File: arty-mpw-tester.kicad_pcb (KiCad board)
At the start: 4 copper layers, 53.3 x 61.5 mm, 144 parts, among them J1 USB4105-GF-A, J10 61300211121, J11 61300211121, J12 61300211121, J14 61300311121, J15 61300311121, J18 61300411121, J19 61300711121, J20 61300411121, J3 arty_chipKIT_connector, J4 61300211121, J5 61300311121, J6 61300211121, J7 61300211121, J8 61300211121, J9 61300211121, Q1 DTC014TEBTL, SW1 JS202011JCQN, SW2 JS202011JCQN, SW3 JS202011JCQN, U1 SN74LVC1G125DCKR, U10 TPD4E02B04DQA, U2 FT232HQ, U3 SN74LVC1G125DCKR, U4 MAX811REUS+T, U5 NTS0102DP, U6 MCP4661-103E/ML, U7 Caravel_breakout_PCB, U8 W25Q32FVSS, U9 MIC2211-AAYML-TR, Y1 ABM8G-12.000MHZ-18-D2Y-T, Y2 ECS-2520MVLC-100-BN-TR

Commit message: Update naming convention
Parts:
- C1, C10, C11, C12, C13, C14, C15, C16, C17, C18, C19, C2, C20, C21, C22, C23, C24, C25, C26, C27, C28, C29, C3, C30, C31, C32, C33, C34, C35, C36, C37, C4, C5, C6, C7, C8, C9: footprint mpw-tester-arty-expansion-footprints:0603-cap -> arty-mpw-tester-footprints:0603-cap
- D1, D2, D3, D4: footprint mpw-tester-arty-expansion-footprints:LED_0603 -> arty-mpw-tester-footprints:LED_0603
- D5, D6, D9: footprint mpw-tester-arty-expansion-footprints:SOD-323F -> arty-mpw-tester-footprints:SOD-323F
- D7, D8: footprint mpw-tester-arty-expansion-footprints:SOD-123 -> arty-mpw-tester-footprints:SOD-123
- J1: footprint mpw-tester-arty-expansion-footprints:GCT_USB4105-GF-A -> arty-mpw-tester-footprints:GCT_USB4105-GF-A
- J10, J11, J12, J4, J6, J7, J8, J9: footprint mpw-tester-arty-expansion-footprints:PinHeader_1x2_P2.54_Drill0.9mm -> arty-mpw-tester-footprints:PinHeader_1x2_P2.54_Drill0.9mm
- J14, J15, J5: footprint mpw-tester-arty-expansion-footprints:PinHeader_1x3_P2.54_Drill1.1mm -> arty-mpw-tester-footprints:PinHeader_1x3_P2.54_Drill1.1mm
- J18, J20: footprint mpw-tester-arty-expansion-footprints:PinHeader_1x4_P2.54mm_Drill1.02mm -> arty-mpw-tester-footprints:PinHeader_1x4_P2.54mm_Drill1.02mm
- J19: footprint mpw-tester-arty-expansion-footprints:61300711121 -> arty-mpw-tester-footprints:61300711121
- J3: footprint mpw-tester-arty-expansion-footprints:ARTY_A7_SHIELD -> arty-mpw-tester-footprints:ARTY_A7_SHIELD
- Q1: footprint mpw-tester-arty-expansion-footprints:SOT-416 -> arty-mpw-tester-footprints:SOT-416
- R1, R10, R11, R12, R13, R14, R15, R16, R17, R18, R19, R2, R20, R21, R22, R23, R24, R25, R26, R27, R28, R29, R3, R30, R31, R32, R33, R34, R35, R6, R7, R8, R9: footprint mpw-tester-arty-expansion-footprints:0603-res -> arty-mpw-tester-footprints:0603-res
- R4, R5: footprint mpw-tester-arty-expansion-footprints:0402-res -> arty-mpw-tester-footprints:0402-res
- S1: footprint mpw-tester-arty-expansion-footprints:SW_SPST_4.2x2.8 -> arty-mpw-tester-footprints:SW_SPST_4.2x2.8
- SW1, SW2, SW3: footprint mpw-tester-arty-expansion-footprints:JS202011JCQN -> arty-mpw-tester-footprints:JS202011JCQN
- TP1: footprint mpw-tester-arty-expansion-footprints:PROBE_PAD_1206 -> arty-mpw-tester-footprints:PROBE_PAD_1206
- U1, U3: footprint mpw-tester-arty-expansion-footprints:SOT-353 -> arty-mpw-tester-footprints:SOT-353
- U10: footprint mpw-tester-arty-expansion-footprints:USON-10_2.5x1.0mm_P0.5mm -> arty-mpw-tester-footprints:USON-10_2.5x1.0mm_P0.5mm
- U2: footprint mpw-tester-arty-expansion-footprints:QFN-48-1EP_8x8mm_P0.5mm_EP6.2x6.2mm_FT232HQ_marking -> arty-mpw-tester-footprints:QFN-48-1EP_8x8mm_P0.5mm_EP6.2x6.2mm_FT232HQ_marking
- U4: footprint mpw-tester-arty-expansion-footprints:SOT-143-4 -> arty-mpw-tester-footprints:SOT-143-4
- U5: footprint mpw-tester-arty-expansion-footprints:TSSOP-8_W3mm -> arty-mpw-tester-footprints:TSSOP-8_W3mm
- U6: footprint mpw-tester-arty-expansion-footprints:QFN-16_EP_4x4_Pitch0.65mm -> arty-mpw-tester-footprints:QFN-16_EP_4x4_Pitch0.65mm
- U7: footprint mpw-tester-arty-expansion-footprints:caravel_breakout -> arty-mpw-tester-footprints:caravel_breakout
- U8: footprint mpw-tester-arty-expansion-footprints:SOIC127P790X216-8N -> arty-mpw-tester-footprints:SOIC127P790X216-8N
- U9: footprint mpw-tester-arty-expansion-footprints:DFN-10-1EP_3x3mm -> arty-mpw-tester-footprints:DFN-10-1EP_3x3mm
- Y1: footprint mpw-tester-arty-expansion-footprints:KX-7 -> arty-mpw-tester-footprints:KX-7
- Y2: footprint mpw-tester-arty-expansion-footprints:Oscillator_SMD_ECS_2520MV-xxx-xx-4Pin_2.5x2.0mm -> arty-mpw-tester-footprints:Oscillator_SMD_ECS_2520MV-xxx-xx-4Pin_2.5x2.0mm

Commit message: Update caravel-breakout footprint with more detailed 3D model and flexypins
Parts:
- G***: footprint antmicro-footprints:antmicro-logo_scaled_12mm_mask -> arty-mpw-tester-footprints:antmicro-logo_scaled_12mm_mask
- G***: footprint antmicro-footprints:antmicro-logo_scaled_12mm -> arty-mpw-tester-footprints:antmicro-logo_scaled_12mm
- REF**: footprint antmicro-footprints:OSHW-Logo_5.7x6mm_Copper -> arty-mpw-tester-footprints:OSHW-Logo_5.7x6mm_Copper
- REF**: footprint antmicro-footprints:OSHW-Logo_5.7x6mm_Mask -> arty-mpw-tester-footprints:OSHW-Logo_5.7x6mm_Mask
- U7: value Caravel_breakout_PCB -> Caravel_breakout_PCB_flexypin; footprint arty-mpw-tester-footprints:caravel_breakout -> arty-mpw-tester-footprints:caravel-breakout-flexypin

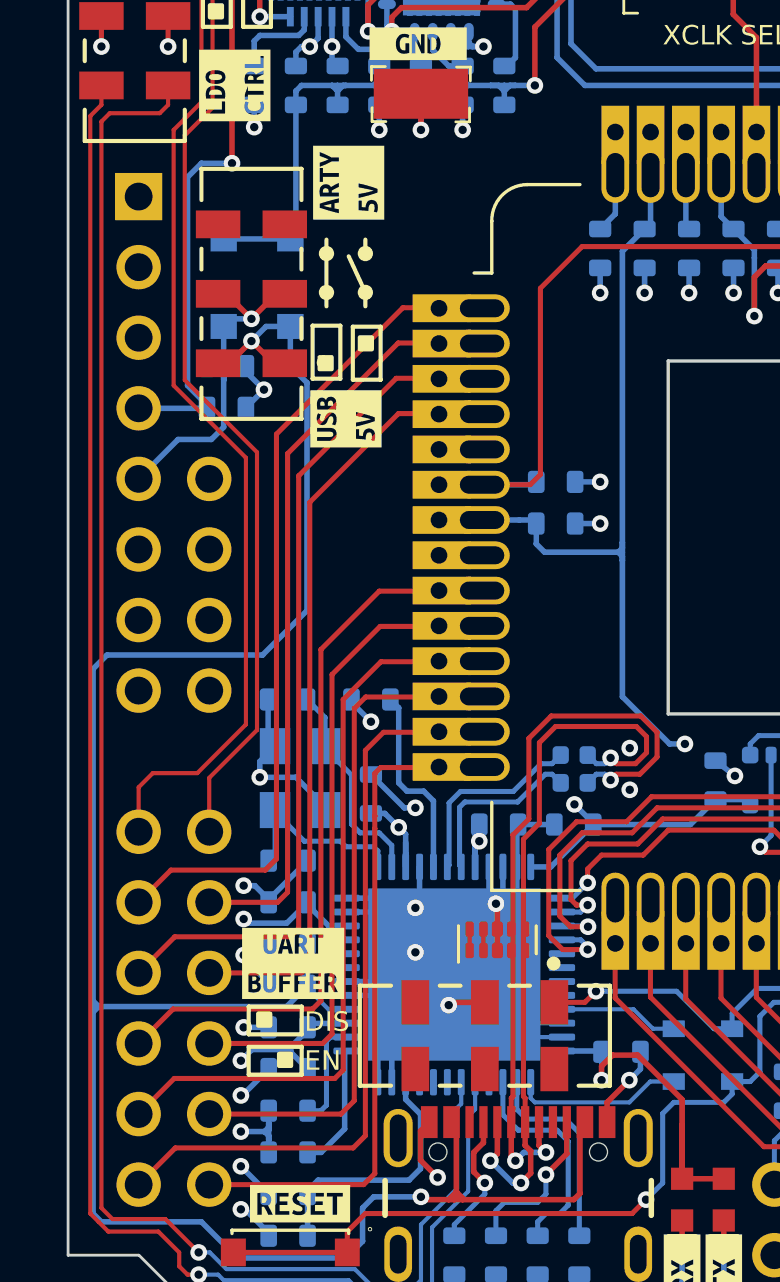
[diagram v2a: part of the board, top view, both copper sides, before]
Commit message: Rotate slide switches so 3D models match default configuration. Update Arty A7 shield connector side
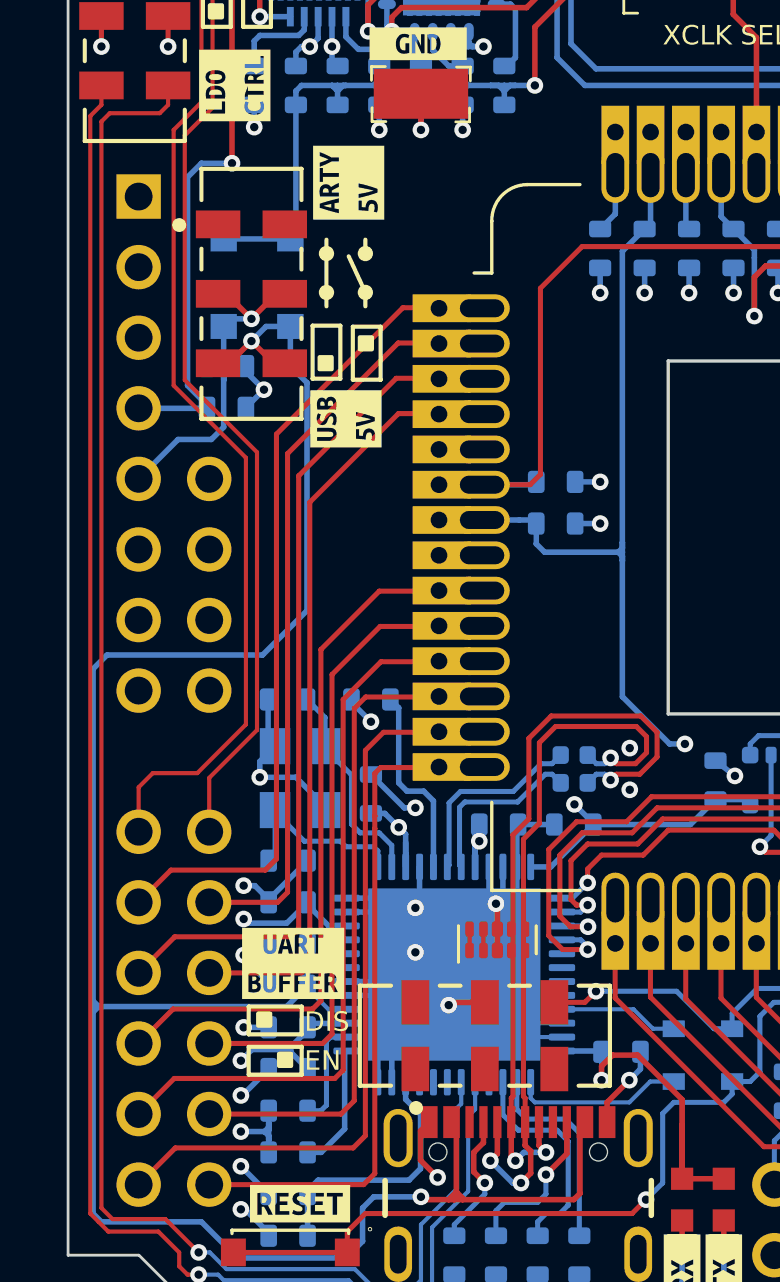
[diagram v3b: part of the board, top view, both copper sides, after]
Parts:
- J3: moved to B.Cu
- turned J3 to 180 degrees
- turned SW2 to 0 degrees
- turned SW3 to -90 degrees
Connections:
- SW2 pad 1: /~{UART_EN} -> unconnected-(SW2-Pad1)
- SW2 pad 2: AGND -> unconnected-(SW2-Pad2)
- SW2 pad 6: unconnected-(SW2-Pad6) -> AGND
- SW2 pad 7: unconnected-(SW2-Pad7) -> /~{UART_EN}
- SW3 pad 1: VBUS -> unconnected-(SW3-Pad1)
- SW3 pad 3: unconnected-(SW3-Pad3) -> VBUS
- SW3 pad 5: VBUS -> unconnected-(SW3-Pad5)
- SW3 pad 7: unconnected-(SW3-Pad7) -> VBUS

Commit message: Add jumper models to the PCB
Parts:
- added REF**: Jumper_1x2_P2.54, arty-mpw-tester-footprints:Jumper_1x2_P2.54, F.Cu at (146.9, 78.9)
- added REF**: Jumper_1x2_P2.54, arty-mpw-tester-footprints:Jumper_1x2_P2.54, F.Cu at (136.3, 67.7)
- added REF**: Jumper_1x2_P2.54, arty-mpw-tester-footprints:Jumper_1x2_P2.54, F.Cu at (124.7, 70.9)
- added REF**: Jumper_1x2_P2.54, arty-mpw-tester-footprints:Jumper_1x2_P2.54, F.Cu at (124.7, 67.7)
- added REF**: Jumper_1x2_P2.54, arty-mpw-tester-footprints:Jumper_1x2_P2.54, F.Cu at (149.5, 67.7)
- added REF**: Jumper_1x2_P2.54, arty-mpw-tester-footprints:Jumper_1x2_P2.54, F.Cu at (141.3, 67.7)
- added REF**: Jumper_1x2_P2.54, arty-mpw-tester-footprints:Jumper_1x2_P2.54, F.Cu at (138.8, 67.7)
- added REF**: Jumper_1x2_P2.54, arty-mpw-tester-footprints:Jumper_1x2_P2.54, F.Cu at (152.1, 67.7)
- added REF**: Jumper_1x2_P2.54, arty-mpw-tester-footprints:Jumper_1x2_P2.54, F.Cu at (147.0, 67.7)
- added REF**: Jumper_1x2_P2.54, arty-mpw-tester-footprints:Jumper_1x2_P2.54, F.Cu at (144.5, 67.7)

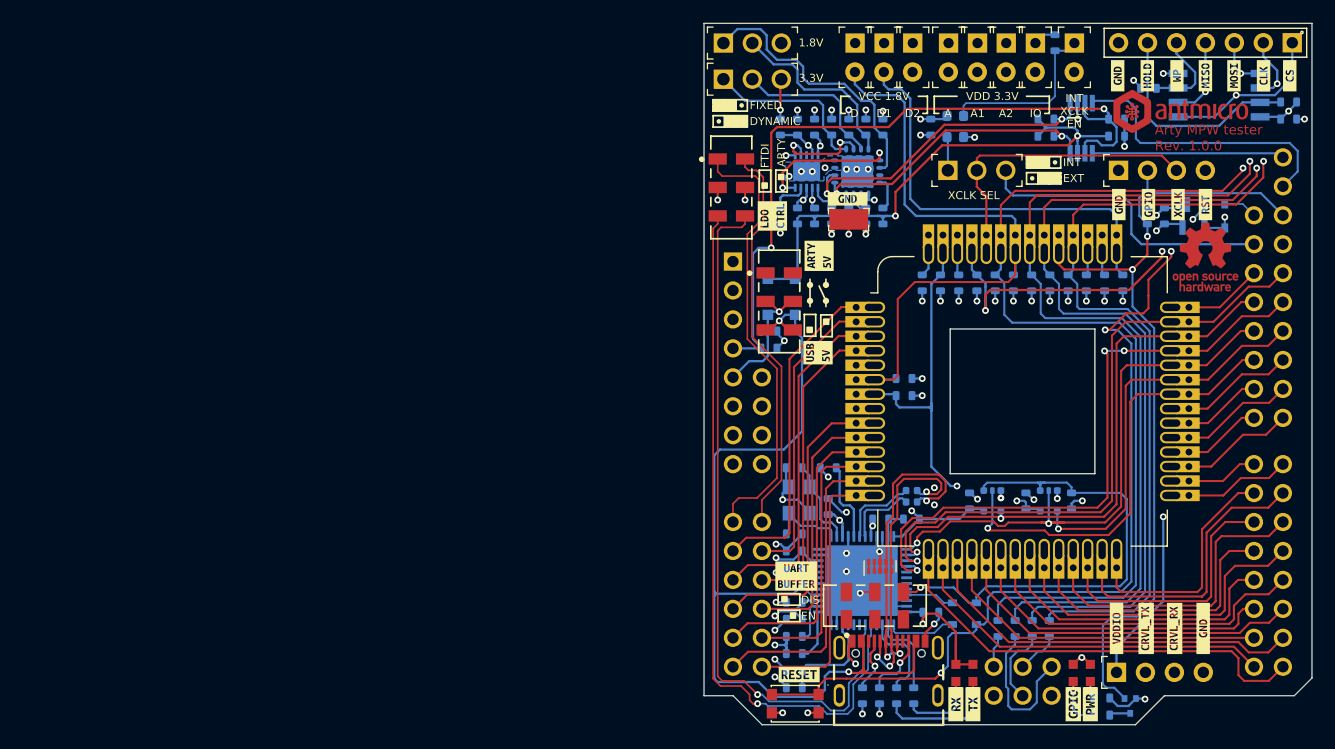
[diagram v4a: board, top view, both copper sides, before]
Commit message: Imported all changes to PCB. Cleared old tracks. Started placement and layout
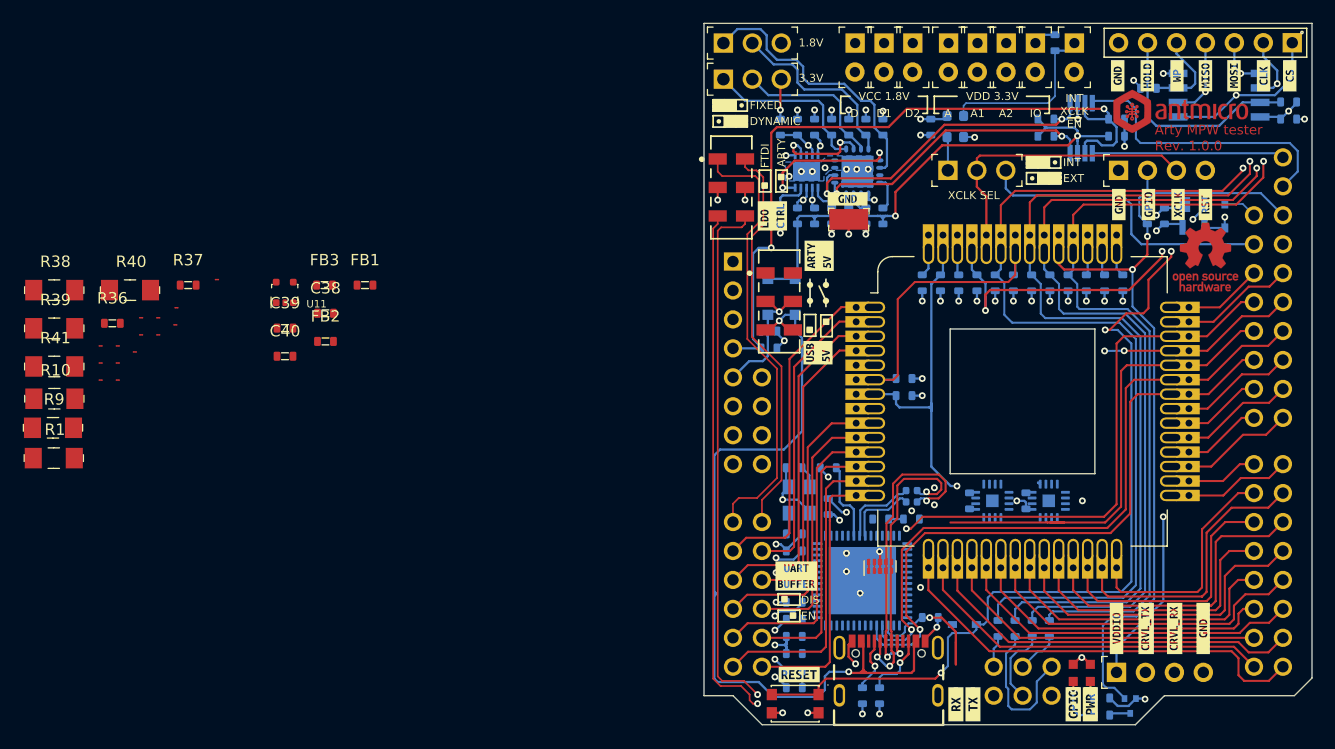
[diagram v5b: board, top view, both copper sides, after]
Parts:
- removed D1, D2: KP-1608ZGC, arty-mpw-tester-footprints:LED_0603
- removed D5: PMEG6002EJ,115, arty-mpw-tester-footprints:SOD-323F
- removed SW2: JS202011JCQN, arty-mpw-tester-footprints:JS202011JCQN
- added C38: C_100n_0603, arty-mpw-tester-footprints:0603-cap, F.Cu at (89.8, 91.4)
- added C39: C_100n_0603, arty-mpw-tester-footprints:0603-cap, F.Cu at (86.2, 92.7)
- added C40: C_100n_0603, arty-mpw-tester-footprints:0603-cap, F.Cu at (86.2, 95.2)
- added FB1: BLM18SG121TN1D, antmicro-footprints:0603-res, F.Cu at (93.2, 89.0)
- added FB2: BLM18SG121TN1D, antmicro-footprints:0603-res, F.Cu at (89.8, 93.9)
- added FB3: BLM18SG121TN1D, antmicro-footprints:0603-res, F.Cu at (89.7, 89.0)
- added NT1: NetTie_2, antmicro-footprints:NetTie-2_SMD_Pad0.127mm, F.Cu at (76.7, 91.0)
- added NT10: NetTie_2, antmicro-footprints:NetTie-2_SMD_Pad0.127mm, F.Cu at (70.1, 95.8)
- added NT11: NetTie_2, antmicro-footprints:NetTie-2_SMD_Pad0.127mm, F.Cu at (70.1, 97.3)
- added NT12: NetTie_2, antmicro-footprints:NetTie-2_SMD_Pad0.127mm, F.Cu at (73.6, 91.8)
- added NT13: NetTie_2, antmicro-footprints:NetTie-2_SMD_Pad0.127mm, F.Cu at (71.6, 97.3)
- added NT14: NetTie_2, antmicro-footprints:NetTie-2_SMD_Pad0.127mm, F.Cu at (75.1, 91.8)
- added NT2: NetTie_2, antmicro-footprints:NetTie-2_SMD_Pad0.127mm, F.Cu at (71.6, 95.8)
- added NT3: NetTie_2, antmicro-footprints:NetTie-2_SMD_Pad0.127mm, F.Cu at (76.6, 92.5)
- added NT4: NetTie_2, antmicro-footprints:NetTie-2_SMD_Pad0.127mm, F.Cu at (73.1, 94.8)
- added NT5: NetTie_2, antmicro-footprints:NetTie-2_SMD_Pad0.127mm, F.Cu at (75.1, 93.3)
- added NT6: NetTie_2, antmicro-footprints:NetTie-2_SMD_Pad0.127mm, F.Cu at (71.6, 94.3)
- added NT7: NetTie_2, antmicro-footprints:NetTie-2_SMD_Pad0.127mm, F.Cu at (73.6, 93.3)
- added NT8: NetTie_2, antmicro-footprints:NetTie-2_SMD_Pad0.127mm, F.Cu at (80.3, 88.5)
- added NT9: NetTie_2, antmicro-footprints:NetTie-2_SMD_Pad0.127mm, F.Cu at (70.1, 94.3)
- added R36: R_10k_0603, arty-mpw-tester-footprints:0603-res, F.Cu at (71.1, 92.3)
- added R37: R_10k_0603, arty-mpw-tester-footprints:0603-res, F.Cu at (77.7, 89.0)
- added R38: R_0R01_1206, antmicro-footprints:1206-res, F.Cu at (66.0, 89.4)
- added R39: R_0R01_1206, antmicro-footprints:1206-res, F.Cu at (66.0, 92.8)
- added R40: R_0R01_1206, antmicro-footprints:1206-res, F.Cu at (72.6, 89.4)
- added R41: R_0R01_1206, antmicro-footprints:1206-res, F.Cu at (66.0, 96.1)
- added U11: TAR5S33UTE85LF, antmicro-footprints:SOT-353, F.Cu at (86.2, 89.6)
- C10, C14, C5, C7: value C_100n_0603 -> C_4u7_0603
- C12: value C_4u7_0603 -> C_1u_0603
- C15: value C_100n_0603 -> C_10n_0603
- C2: value C_4u7_0603 -> C_100n_0603
- C8: value C_100n_0603 -> C_10u_0603; footprint arty-mpw-tester-footprints:0603-cap -> antmicro-footprints:0603-cap
- R1: value R_10k_0603 -> R_0R01_1206; footprint arty-mpw-tester-footprints:0603-res -> antmicro-footprints:1206-res; moved to F.Cu
- R10, R9: value R_470R_0603 -> R_0R01_1206; footprint arty-mpw-tester-footprints:0603-res -> antmicro-footprints:1206-res; moved to F.Cu
- U1, U3: value SN74LVC1G125DCKR -> PAC1954T-E/4MX; footprint arty-mpw-tester-footprints:SOT-353 -> antmicro-footprints:VQFN-16-1EP_3x3mm_P0.5mm_EP1.1x1.1mm
- U2: value FT232HQ -> FT4232H-56Q; footprint arty-mpw-tester-footprints:QFN-48-1EP_8x8mm_P0.5mm_EP6.2x6.2mm_FT232HQ_marking -> antmicro-footprints:QFN-56-1EP_8x8mm_P0.5mm_EP5.5.9x5.9mm
- moved R1 89.4 mm to (65.9, 104.2), turned to 0 degrees
- moved R9 79.1 mm to (65.9, 101.5), turned to 0 degrees
- moved R10 78.4 mm to (66.0, 98.9), turned to 0 degrees
- moved C16 0.46 mm to (142.8, 118.1)
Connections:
- net /CC1 renamed /FTDI/CC1
- net /CC2 renamed /FTDI/CC2
- net /CRVL_IO0 renamed CRVL_IO0
- net /CRVL_IO10 renamed CRVL_IO10
- net /CRVL_IO11 renamed CRVL_IO11
- net /CRVL_IO12 renamed CRVL_IO12
- net /CRVL_IO13 renamed CRVL_IO13
- net /CRVL_IO14 renamed CRVL_IO14
- net /CRVL_IO15 renamed CRVL_IO15
- net /CRVL_IO16 renamed CRVL_IO16
- net /CRVL_IO17 renamed CRVL_IO17
- net /CRVL_IO18 renamed CRVL_IO18
- net /CRVL_IO19 renamed CRVL_IO19
- net /CRVL_IO20 renamed CRVL_IO20
- net /CRVL_IO21 renamed CRVL_IO21
- net /CRVL_IO22 renamed CRVL_IO22
- net /CRVL_IO23 renamed CRVL_IO23
- net /CRVL_IO24 renamed CRVL_IO24
- net /CRVL_IO25 renamed CRVL_IO25
- net /CRVL_IO26 renamed CRVL_IO26
- net /CRVL_IO27 renamed CRVL_IO27
- net /CRVL_IO28 renamed CRVL_IO28
- net /CRVL_IO29 renamed CRVL_IO29
- net /CRVL_IO30 renamed CRVL_IO30
- net /CRVL_IO31 renamed CRVL_IO31
- net /CRVL_IO32 renamed CRVL_IO32
- net /CRVL_IO33 renamed CRVL_IO33
- net /CRVL_IO34 renamed CRVL_IO34
- net /CRVL_IO35 renamed CRVL_IO35
- net /CRVL_IO36 renamed CRVL_IO36
- net /CRVL_IO37 renamed CRVL_IO37
- net /CRVL_IO7 renamed CRVL_IO7
- net /CRVL_IO8 renamed CRVL_IO8
- net /CRVL_IO9 renamed CRVL_IO9
- net /MEM.~{HOLD} renamed MEM.~{HOLD}
- net /MEM.~{WP} renamed MEM.~{WP}
- net /USB_DN renamed /FTDI/USB_DN
- net /USB_DP renamed /FTDI/USB_DP
- C1 pad 2: AGND -> EP
- C10 pad 1: +3V3 -> /FTDI/VPLL
- C10 pad 2: AGND -> EP
- C11 pad 1: /VCORE -> /FTDI/VPLL
- C11 pad 2: AGND -> EP
- C12 pad 1: /FTDI_3V3 -> VBUS
- C12 pad 2: AGND -> EP
- C13 pad 1: /FTDI_3V3 -> 3V3_FTDI
- C13 pad 2: AGND -> EP
- C14 pad 1: /VCCA -> /FTDI/VCORE
- C14 pad 2: AGND -> EP
- C15 pad 1: /FTDI_3V3 -> Net-(C15-Pad1)
- C15 pad 2: AGND -> EP
- C16 pad 1: /FTDI_3V3 -> /FTDI/VCORE
- C16 pad 2: AGND -> EP
- C17 pad 1: /FTDI_RESET -> /FTDI/FTDI_RST
- C17 pad 2: AGND -> EP
- C18 pad 1: /FTDI_3V3 -> /FTDI/VCORE
- C18 pad 2: AGND -> EP
- C19 pad 2: AGND -> EP
- C2 pad 1: VBUS -> 3V3_FTDI
- C2 pad 2: AGND -> EP
- C20 pad 2: AGND -> EP
- C21 pad 2: AGND -> EP
- C22 pad 2: AGND -> EP
- C23 pad 2: AGND -> EP
- C24 pad 2: AGND -> EP
- C25 pad 2: AGND -> EP
- C26 pad 2: AGND -> EP
- C27 pad 2: AGND -> EP
- C28 pad 2: AGND -> EP
- C29 pad 2: AGND -> EP
- C3 pad 2: AGND -> EP
- C30 pad 2: AGND -> EP
- C31 pad 2: AGND -> EP
- C32 pad 2: AGND -> EP
- C33 pad 2: AGND -> EP
- C34 pad 2: AGND -> EP
- C35 pad 2: AGND -> EP
- C36 pad 2: AGND -> EP
- C37 pad 2: AGND -> EP
- C4 pad 1: /FTDI_3V3 -> 3V3_FTDI
- C4 pad 2: AGND -> EP
- C5 pad 1: /FTDI_3V3 -> /FTDI/VPHY
- C5 pad 2: AGND -> EP
- C6 pad 1: /XIN -> /FTDI/XIN
- C6 pad 2: AGND -> EP
- C7 pad 1: VBUS -> /FTDI/VPHY
- C7 pad 2: AGND -> EP
- C8 pad 1: /FTDI_3V3 -> Net-(FB3-Pad1)
- C8 pad 2: AGND -> EP
- C9 pad 1: /XOUT -> /FTDI/XOUT
- C9 pad 2: AGND -> EP
- D6 pad K: /FTDI_~{MR} -> FTDI_~{MR}
- J1 pad A1: AGND -> EP
- J1 pad A12: AGND -> EP
- J1 pad B1: AGND -> EP
- J1 pad B12: AGND -> EP
- J1 pad S1: AGND -> EP
- J10 pad 2: /VCCD -> Net-(J10-Pad2)
- J11 pad 2: /VCCD1 -> Net-(J11-Pad2)
- J12 pad 2: /VCCD2 -> Net-(J12-Pad2)
- J18 pad 2: /CRVL_IO5 -> CRVL_IO5
- J18 pad 3: /CRVL_IO6 -> CRVL_IO6
- J18 pad 4: AGND -> EP
- J19 pad 1: /MEM.~{CS} -> MEM.~{CS}
- J19 pad 2: /MEM.SCK -> MEM.SCK
- J19 pad 3: /MEM.SI -> MEM.SI
- J19 pad 4: /MEM.SO -> MEM.SO
- J19 pad 7: AGND -> EP
- J20 pad 1: AGND -> EP
- J3 pad 17: AGND -> EP
- J3 pad 26: AGND -> EP
- J3 pad 34: /CRVL_IO2 -> CRVL_IO2
- J3 pad 35: /CRVL_IO4 -> CRVL_IO4
- J3 pad 36: /CRVL_IO6 -> CRVL_IO6
- J3 pad 50: AGND -> EP
- J3 pad 51: /CRVL_IO1 -> CRVL_IO1
- J3 pad 52: /CRVL_IO3 -> CRVL_IO3
- J3 pad 53: /CRVL_IO5 -> CRVL_IO5
- J3 pad 6: AGND -> EP
- J3 pad 7: AGND -> EP
- J4 pad 2: AGND -> EP
- J6 pad 2: /VDDA -> Net-(J6-Pad2)
- J7 pad 2: /VDDIO -> Net-(J7-Pad2)
- J8 pad 2: /VDDA2 -> Net-(J8-Pad2)
- J9 pad 2: /VDDA1 -> Net-(J9-Pad2)
- Q1 pad 2: AGND -> EP
- R1 pad 1: /~{UART_EN} -> Net-(J7-Pad2)
- R1 pad 2: +3V3 -> /VDDIO
- R10 pad 1: /~{TX_LED} -> Net-(J12-Pad2)
- R10 pad 2: Net-(D2-Pad2) -> /VCCD2
- R11 pad 2: /MEM.SCK -> MEM.SCK
- R13 pad 1: AGND -> EP
- R14 pad 2: /MEM.SO -> MEM.SO
- R15 pad 2: /MEM.SI -> MEM.SI
- R17 pad 2: /MEM.~{CS} -> MEM.~{CS}
- R18 pad 2: /MEM.SCK -> MEM.SCK
- R19 pad 2: /MEM.SI -> MEM.SI
- R2 pad 2: AGND -> EP
- R21 pad 2: /MEM.SO -> MEM.SO
- R23 pad 1: AGND -> EP
- R25 pad 1: AGND -> EP
- R29 pad 1: AGND -> EP
- R3 pad 2: AGND -> EP
- R4 pad 2: /FTDI_DN -> /FTDI/FTDI_DN
- R5 pad 2: /FTDI_DP -> /FTDI/FTDI_DP
- R6 pad 1: /FTDI_3V3 -> 3V3_FTDI
- R6 pad 2: /FTDI_RESET -> /FTDI/FTDI_RST
- R7 pad 1: AGND -> EP
- R7 pad 2: /REF -> /FTDI/REF
- R8 pad 2: /MEM.~{CS} -> MEM.~{CS}
- R9 pad 1: /~{RX_LED} -> Net-(J11-Pad2)
- R9 pad 2: Net-(D1-Pad2) -> /VCCD1
- S1 pad 2: AGND -> EP
- S1 pad 4: AGND -> EP
- SW1 pad 3: /FTDI_EN_VOUT1 -> FTDI_EN_VOUT1
- SW1 pad 7: /FTDI_EN_VOUT2 -> FTDI_EN_VOUT2
- TP1 pad 1: AGND -> EP
- U1 pad 1: /~{UART_EN} -> EP
- U1 pad 2: /CRVL_IO4 -> 3V3_FTDI
- U1 pad 3: AGND -> EP
- U1 pad 4: /CRVL_IO5 -> /ARTY_SCL_3V3
- U1 pad 5: +3V3 -> /ARTY_SDA_3V3
- U10 pad 3: AGND -> EP
- U10 pad 8: AGND -> EP
- U2 pad 1: /XIN -> unconnected-(U2-Pad1)
- U2 pad 10: AGND -> EP
- U2 pad 11: AGND -> /FTDI/FTDI_RST
- U2 pad 12: /FTDI_3V3 -> CRVL_IO4
- U2 pad 13: /CRVL_IO4 -> CRVL_IO2
- U2 pad 14: /CRVL_IO2 -> CRVL_IO1
- U2 pad 15: /CRVL_IO1 -> CRVL_IO3
- U2 pad 16: /CRVL_IO3 -> 3V3_FTDI
- U2 pad 2: /XOUT -> /FTDI/VCORE
- U2 pad 21: /FTDI_~{UART_EN} -> EP
- U2 pad 22: AGND -> MEM.SCK
- U2 pad 23: AGND -> MEM.SO
- U2 pad 24: /FTDI_3V3 -> MEM.SI
- U2 pad 25: /FTDI_~{MR} -> MEM.~{CS}
- U2 pad 26: /~{RX_LED} -> FTDI_~{MR}
- U2 pad 27: /~{TX_LED} -> FTDI_EN_VOUT1
- U2 pad 28: unconnected-(U2-Pad28) -> FTDI_EN_VOUT2
- U2 pad 29: /FTDI_EN_VOUT1 -> unconnected-(U2-Pad29)
- U2 pad 3: /FTDI_3V3 -> /FTDI/XIN
- U2 pad 30: /FTDI_EN_VOUT2 -> unconnected-(U2-Pad30)
- U2 pad 31: unconnected-(U2-Pad31) -> /FTDI/VCORE
- U2 pad 32: unconnected-(U2-Pad32) -> CRVL_IO5
- U2 pad 33: unconnected-(U2-Pad33) -> CRVL_IO6
- U2 pad 34: /FTDI_RESET -> unconnected-(U2-Pad34)
- U2 pad 35: AGND -> unconnected-(U2-Pad35)
- U2 pad 36: AGND -> 3V3_FTDI
- U2 pad 37: /VCCA -> unconnected-(U2-Pad37)
- U2 pad 38: /VCORE -> unconnected-(U2-Pad38)
- U2 pad 39: /FTDI_3V3 -> unconnected-(U2-Pad39)
- U2 pad 4: AGND -> /FTDI/XOUT
- U2 pad 40: VBUS -> unconnected-(U2-Pad40)
- U2 pad 41: AGND -> EP
- U2 pad 42: AGND -> unconnected-(U2-Pad42)
- U2 pad 43: unconnected-(U2-Pad43) -> /FTDI/VCORE
- U2 pad 44: unconnected-(U2-Pad44) -> 3V3_FTDI
- U2 pad 45: unconnected-(U2-Pad45) -> EP
- U2 pad 46: /FTDI_3V3 -> unconnected-(U2-Pad46)
- U2 pad 47: AGND -> unconnected-(U2-Pad47)
- U2 pad 48: AGND -> unconnected-(U2-Pad48)
- U2 pad 49: AGND -> unconnected-(U2-Pad49)
- U2 pad 5: /REF -> /FTDI/VPHY
- U2 pad 6: /FTDI_DN -> /FTDI/REF
- U2 pad 7: /FTDI_DP -> /FTDI/FTDI_DN
- U2 pad 8: /FTDI_3V3 -> /FTDI/FTDI_DP
- U2 pad 9: AGND -> /FTDI/VPLL
- U3 pad 1: /~{UART_EN} -> EP
- U3 pad 2: /CRVL_IO6 -> 3V3_FTDI
- U3 pad 3: AGND -> EP
- U3 pad 4: /CRVL_IO2 -> /ARTY_SCL_3V3
- U3 pad 5: /FTDI_3V3 -> /ARTY_SDA_3V3
- U4 pad 1: AGND -> EP
- U5 pad 2: AGND -> EP
- U6 pad 13: AGND -> EP
- U6 pad 14: AGND -> EP
- U6 pad 17: AGND -> EP
- U6 pad 3: AGND -> EP
- U6 pad 4: AGND -> EP
- U7 pad 36: /CRVL_IO6 -> CRVL_IO6
- U7 pad 37: /CRVL_IO5 -> CRVL_IO5
- U7 pad 38: /CRVL_IO4 -> CRVL_IO4
- U7 pad 39: /CRVL_IO3 -> CRVL_IO3
- U7 pad 40: /CRVL_IO2 -> CRVL_IO2
- U7 pad 41: /CRVL_IO1 -> CRVL_IO1
- U7 pad 46: /MEM.SCK -> MEM.SCK
- U7 pad 48: /MEM.SO -> MEM.SO
- U7 pad 49: /MEM.SI -> MEM.SI
- U7 pad 5: AGND -> EP
- U7 pad 51: /MEM.~{CS} -> MEM.~{CS}
- U7 pad 8: AGND -> EP
- U8 pad 1: /MEM.~{CS} -> MEM.~{CS}
- U8 pad 2: /MEM.SO -> MEM.SO
- U8 pad 4: AGND -> EP
- U8 pad 5: /MEM.SI -> MEM.SI
- U8 pad 6: /MEM.SCK -> MEM.SCK
- U9 pad 11: AGND -> EP
- U9 pad 6: AGND -> EP
- Y1 pad 1: /XIN -> /FTDI/XIN
- Y1 pad 2: AGND -> EP
- Y1 pad 3: /XOUT -> /FTDI/XOUT
- Y1 pad 4: AGND -> EP
- Y2 pad 2: AGND -> EP
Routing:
- net AGND: track 130.7 -> 0.00 mm, vias 60 -> 0
- net /MEM.~{CS}: track 102.3 -> 0.00 mm, vias 2 -> 0
- net MEM.~{CS}: track 0.00 -> 102.2 mm, vias 0 -> 2
- net CRVL_IO6: track 0.00 -> 100.0 mm, vias 0 -> 1
- net MEM.SO: track 0.00 -> 91.0 mm, vias 0 -> 2
- net /MEM.SO: track 91.0 -> 0.00 mm, vias 2 -> 0
- net /MEM.SI: track 88.7 -> 0.00 mm, vias 2 -> 0
- net MEM.SI: track 0.00 -> 88.5 mm, vias 0 -> 2
- net MEM.SCK: track 0.00 -> 81.5 mm, vias 0 -> 2
- net /MEM.SCK: track 81.5 -> 0.00 mm, vias 2 -> 0
- net EP: track 0.00 -> 70.4 mm, vias 0 -> 57
- net /CRVL_IO6: track 67.4 -> 0.00 mm, vias 1 -> 0
- net /FTDI_EN_VOUT2: track 63.1 -> 0.00 mm, vias 1 -> 0
- net /FTDI_EN_VOUT1: track 62.8 -> 0.00 mm, vias 1 -> 0
- net CRVL_IO5: track 0.00 -> 59.2 mm, vias 0 -> 1
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- added copper zone on In2.Cu, net /ARTY_SDA_3V3
- added copper zone on B.Cu, net EP
- added copper zone on In1.Cu, net EP
- added copper zone on In2.Cu, net EP
- removed copper zone on In2.Cu, net /FTDI_3V3
- removed copper zone on B.Cu, net AGND
- removed copper zone on In1.Cu, net AGND
- removed copper zone on In2.Cu, net AGND
